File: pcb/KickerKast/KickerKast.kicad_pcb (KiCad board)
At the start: 2 copper layers, 45 x 67.8 mm, 29 parts, among them CON1 BARREL_JACK, P1 SENS1, P2 SENS2, P3 Program, P4 UART, P5 7SEG_1, P6 7SEG_2, Q1 7S1a, Q2 7S1b, Q3 7S2a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

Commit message: added text to kickerkast pcb
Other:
- board text added: "5V"
- board text added: "7-segment 1"
- board text added: "7-segment 2"
- board text added: "gnd"
- board text added: "program"
- board text added: "rx"
- board text added: "sensor 1"
- board text added: "sensor 2"
- board text added: "tx"
- board text added: "uart"
- board text added: "vdd"
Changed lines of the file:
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@@
     (links 91)
     (no_connects 0)
-    (area 0 0 0 0)
+    (area 52.111 62.074379 99.389001 134.615)
     (thickness 1.6)
-    (drawings 4)
+    (drawings 16)
     (tracks 263)
     (zones 0)
@@
   )
   (setup
-    (last_trace_width 0.508)
+    (last_trace_width 0.25)
     (user_trace_width 0.1524)
     (user_trace_width 0.254)
@@
     (descr "Capacitor 3mm Disc, Pitch 2.5mm")
     (tags Capacitor)
-    (fp_text reference C4 (at 1.25 -2.5) (layer F.SilkS)
+    (fp_text reference C4 (at -2.286 0) (layer F.SilkS)
       (effects (font (size 1 1) (thickness 0.15)))
     )
@@
     (fp_arc (start 1.311 0.034) (end 3.051 0.994) (angle 110) (layer F.SilkS) (width 0.15))
     (fp_arc (start 1.301 0.034) (end 2.335 1.094) (angle 87.5) (layer F.SilkS) (width 0.15))
-    (fp_text user K (at -1.69 1.74) (layer F.SilkS)
+    (fp_text user K (at -0.762 -2.794) (layer F.SilkS)
       (effects (font (size 1 1) (thickness 0.15)))
     )
@@
     (descr "Through hole pin header")
     (tags "pin header")
-    (fp_text reference P5 (at 0 -5.1 90) (layer F.SilkS)
+    (fp_text reference P5 (at -1.016 -12.446 90) (layer F.SilkS) hide
       (effects (font (size 1 1) (thickness 0.15)))
     )
@@
     (descr "Resistor, Axial,  RM 10mm, 1/3W")
     (tags "Resistor Axial RM 10mm 1/3W")
-    (fp_text reference R3 (at 5.32892 -3.50012 180) (layer F.SilkS)
+    (fp_text reference R3 (at 5.08 0 180) (layer F.SilkS)
       (effects (font (size 1 1) (thickness 0.15)))
     )
@@
     (descr "28-lead dip package, row spacing 7.62 mm (300 mils), longer pads")
     (tags "dil dip 2.54 300")
-    (fp_text reference U1 (at 0 -5.22 90) (layer F.SilkS)
+    (fp_text reference U1 (at 2.286 -14.224 90) (layer F.SilkS) hide
       (effects (font (size 1 1) (thickness 0.15)))
     )
@@
     (descr "Crystal Quarz HC49/U vertical stehend")
     (tags "Crystal Quarz HC49/U vertical stehend")
-    (fp_text reference Y1 (at 0 -3.81) (layer F.SilkS)
+    (fp_text reference Y1 (at 0 3.302) (layer F.SilkS)
       (effects (font (size 1 1) (thickness 0.15)))
     )
@@
       (net 33 "Net-(U1-Pad10)"))
   )
+  (gr_text program (at 57.15 103.886) (layer F.SilkS)
+    (effects (font (size 0.508 0.508) (thickness 0.127)))
+  )
+  (gr_text vdd (at 97.79 120.65 45) (layer F.SilkS)
+    (effects (font (size 0.508 0.508) (thickness 0.127)))
+  )
+  (gr_text rx (at 97.79 118.11 45) (layer F.SilkS)
+    (effects (font (size 0.508 0.508) (thickness 0.127)))
+  )
+  (gr_text tx (at 97.79 115.57 45) (layer F.SilkS)
+    (effects (font (size 0.508 0.508) (thickness 0.127)))
+  )
+  (gr_text gnd (at 97.79 113.03 45) (layer F.SilkS)
+    (effects (font (size 0.508 0.508) (thickness 0.127)))
+  )
+  (gr_text uart (at 95.25 122.936) (layer F.SilkS)
+    (effects (font (size 0.508 0.508) (thickness 0.127)))
+  )
+  (gr_text "sensor 2" (at 64.516 130.302 90) (layer F.SilkS)
+    (effects (font (size 0.508 0.508) (thickness 0.127)))
+  )
+  (gr_text "sensor 1" (at 55.88 130.302 90) (layer F.SilkS)
+    (effects (font (size 0.508 0.508) (thickness 0.127)))
+  )
+  (gr_text 5V (at 86.36 77.47) (layer F.SilkS)
+    (effects (font (size 0.508 0.508) (thickness 0.127)))
+  )
+  (gr_text gnd (at 77.978 70.358) (layer F.SilkS)
+    (effects (font (size 0.508 0.508) (thickness 0.127)))
+  )
+  (gr_text "7-segment 2" (at 75.438 82.55 90) (layer F.SilkS)
+    (effects (font (size 0.508 0.508) (thickness 0.127)))
+  )
+  (gr_text "7-segment 1" (at 59.944 82.55 90) (layer F.SilkS)
+    (effects (font (size 0.508 0.508) (thickness 0.127)))
+  )
   (gr_line (start 54.356 133.604) (end 54.356 65.786) (angle 90) (layer Edge.Cuts) (width 0.15))

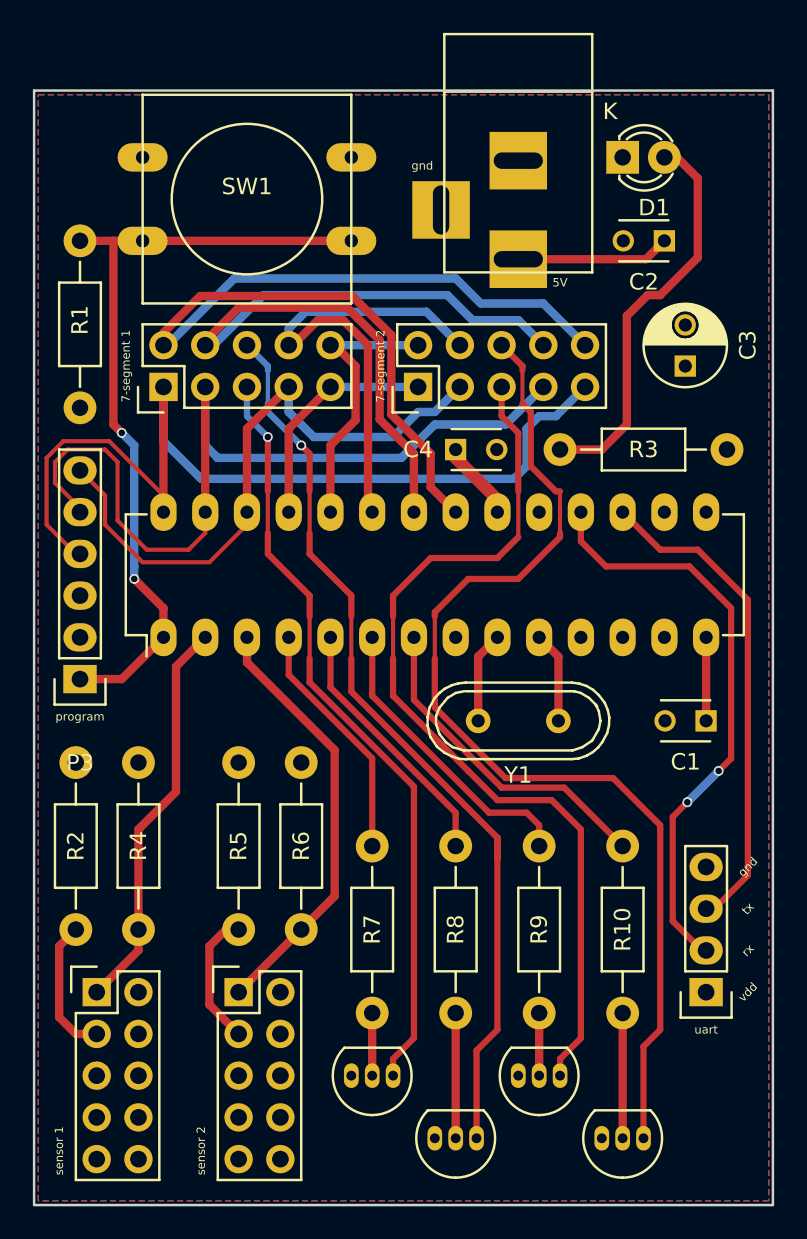
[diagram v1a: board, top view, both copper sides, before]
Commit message: added extra connector to kickerkast pcb
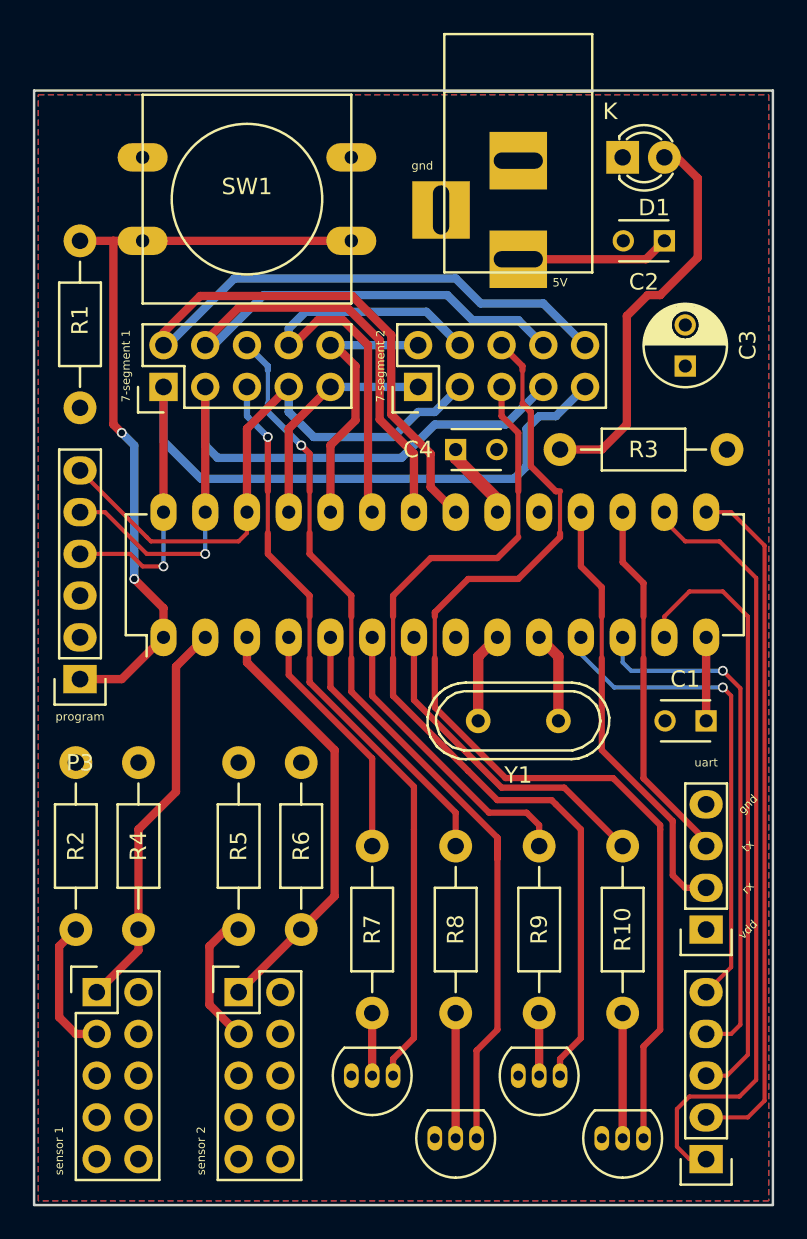
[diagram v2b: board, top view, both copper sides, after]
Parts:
- added P7: CONN_01X05, Pin_Headers:Pin_Header_Straight_1x05, F.Cu at (95.2, 130.8)
- moved P4 3.81 mm to (95.2, 116.8)
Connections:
- U1 pad 11: Net-(U1-Pad11) -> /RC0
- U1 pad 12: Net-(U1-Pad12) -> /RC1
- U1 pad 13: Net-(U1-Pad13) -> /RC2
- U1 pad 15: Net-(U1-Pad15) -> /RC4
- U1 pad 16: Net-(U1-Pad16) -> /RC5
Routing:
- net /RC5: track 0.00 -> 48.0 mm
- net /RC4: track 0.00 -> 42.2 mm
- net /RC2: track 0.00 -> 37.3 mm
- net /RC1: track 0.00 -> 32.1 mm, vias 0 -> 1
- net /RC0: track 0.00 -> 29.9 mm, vias 0 -> 1
- net /RX: track 35.9 -> 26.8 mm, vias 2 -> 0
- net /c: track 53.3 -> 45.3 mm, vias 0 -> 1
- net /TX: track 30.0 -> 22.4 mm
- net /DP: track 57.9 -> 51.1 mm, vias 0 -> 1
- net /d: track 37.7 -> 36.7 mm

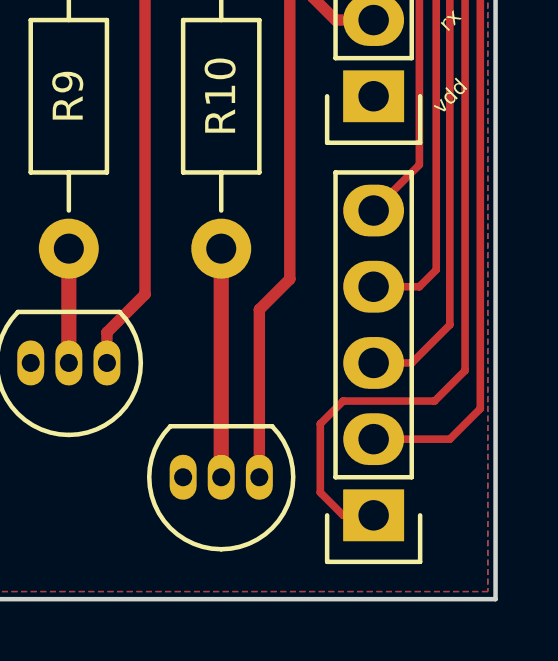
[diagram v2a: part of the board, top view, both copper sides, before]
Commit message: added text to kickerkast pcb
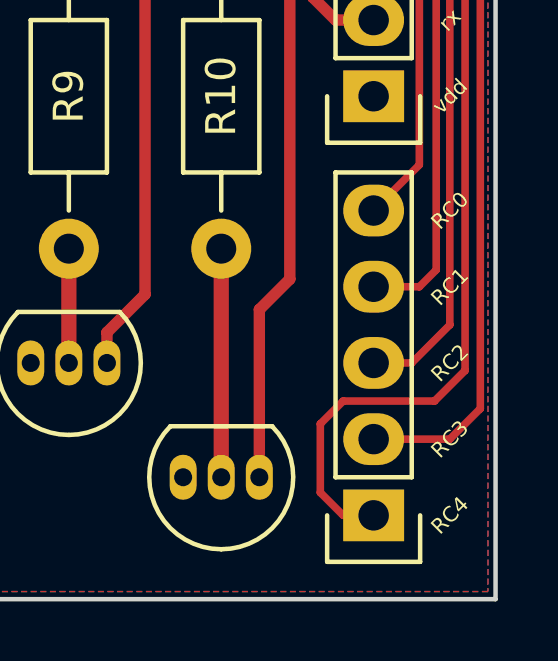
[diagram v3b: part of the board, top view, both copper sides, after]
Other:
- board text added: "RC0"
- board text added: "RC1"
- board text added: "RC2"
- board text added: "RC3"
- board text added: "RC4"
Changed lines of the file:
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@@
     (area 54.280999 65.710999 99.389001 133.679001)
     (thickness 1.6)
-    (drawings 16)
+    (drawings 21)
     (tracks 293)
     (zones 0)
@@
     )
   )
+  (gr_text RC4 (at 97.79 130.81 45) (layer F.SilkS)
+    (effects (font (size 0.508 0.508) (thickness 0.127)))
+  )
+  (gr_text RC3 (at 97.79 128.27 45) (layer F.SilkS)
+    (effects (font (size 0.508 0.508) (thickness 0.127)))
+  )
+  (gr_text RC2 (at 97.79 125.73 45) (layer F.SilkS)
+    (effects (font (size 0.508 0.508) (thickness 0.127)))
+  )
+  (gr_text RC1 (at 97.79 123.19 45) (layer F.SilkS)
+    (effects (font (size 0.508 0.508) (thickness 0.127)))
+  )
+  (gr_text RC0 (at 97.79 120.65 45) (layer F.SilkS)
+    (effects (font (size 0.508 0.508) (thickness 0.127)))
+  )
   (gr_text program (at 57.15 103.886) (layer F.SilkS)
